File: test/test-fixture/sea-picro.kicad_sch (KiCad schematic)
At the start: 89 parts, among them J2 Sea-Picro

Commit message: tester footprints setup
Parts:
- added H1, H2, H3, H4, H5, H6: M3, MountingHole:MountingHole_3.2mm_M3_Pad_Via, symbol Mechanical:MountingHole_Pad
- added N1: Toggle Clamp, josh-mechanical:GH-201A_X_Adj, symbol Mechanical:Housing
- added R10, R11, R12, R13, R14, R15, R16, R17, R18, R19, R20, R21, R22, R23, R24, R25, R26, R27, R28, R29, R30, R31, R32, R4, R5, R9: 0R0, Resistor_SMD:R_0603_1608Metric, symbol Device:R
- C5: renamed from C?; footprint (none) -> Capacitor_SMD:C_0603_1608Metric
- D2, D3: renamed from D?; footprint (none) -> LED_THT:LED_D5.0mm
- J10, J11, J13, J5, J6: renamed from J?; footprint (none) -> Connector_PinHeader_2.54mm:PinHeader_1x03_P2.54mm_Vertical
- J12: renamed from J?; footprint (none) -> josh-connectors:SAMTEC_FTSH-105-01-L-DV-R-TR
- J2: footprint josh-module:Sea-Picro_EXT_Module_Castellated -> josh-module:Sea-Picro_EXT_Pogo_Pins
- J3, J7: renamed from J?; footprint (none) -> Connector_PinHeader_2.54mm:PinHeader_1x02_P2.54mm_Vertical
- J4: renamed from J?; footprint (none) -> Connector_PinSocket_2.54mm:PinSocket_2x20_P2.54mm_Vertical
- J9: renamed from J?; footprint (none) -> josh-module:OLED_SSD1306_I2C_0.96
- R2, R33, R34, R35, R36, R37, R38, R39, R40, R41, R42, R43, R44, R6, R7, R8: renamed from R?; footprint (none) -> Resistor_SMD:R_0603_1608Metric
- SW1, SW2: renamed from SW?; footprint (none) -> josh-buttons-switches:SW_Push_PTS645
- SW3, SW4, SW5, SW6: renamed from SW?; footprint (none) -> josh-buttons-switches:SW_SPDT_PCM12
- TP1, TP2, TP3, TP4: renamed from TP?; footprint (none) -> josh-test-point:TestPoint_Pogo_1.4mm_Drill_Off_Center
- U1: renamed from U?; footprint (none) -> Package_TO_SOT_SMD:SOT-23-6
- gave numbers to parts that had none: 30
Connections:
- net +5V: now also J9.2 (Pin_2); no longer J9.3 (Pin_3)
- net GND: now also J9.1 (Pin_1), H1.1, H2.1, H3.1, H4.1, H5.1, H6.1; no longer J9.4 (Pin_4)
- net I2C_SCL: now also J9.3 (Pin_3), R12.2; no longer J4.5 (SCL/GPIO3), J9.2 (Pin_2)
- net I2C_SDA: now also J9.4 (Pin_4), R10.2; no longer J4.3 (SDA/GPIO2), J9.1 (Pin_1)
- net LED_FAIL: now also R31.2
- net LED_PASS: now also R32.2
- net LOAD_SW_EN: now also R23.1
- net LOAD_SW_nFAULT: now also R21.1
- net RPI_SWDCLK: now also R27.1; no longer J4.22 (GPIO25)
- net RPI_SWDIO: now also R25.1; no longer J4.18 (GPIO24)
- net RPI_nRST: now also R19.1
- net SEL_BOOTLD: now also R24.2
- net SEL_EXT_RST: now also R22.2
- net SEL_FW: now also R26.2
- net SEL_TEST: now also R28.2
- net SHT_CTRL_3V3: now also R20.2
- net SHT_CTRL_5V: now also R18.2
- net SP_BOOT: now also R30.1
- net SP_RUN: now also R29.1
- net SR_CLK: now also R11.1
- net SR_RCLK: now also R15.1
- net SR_SER: now also R9.1
- net SR_nCLR: now also R13.1
- net SR_nOE: now also R17.1
- net SW_FAIL: now also R16.2
- net SW_PASS: now also R14.2
- net at J4.10 (GPIO15/RXD): now also R5.2
- net at J4.11 (GPIO17): now also R11.2
- net at J4.12 (GPIO18/PWM0): now also R13.2
- net at J4.13 (GPIO27): now also R30.2
- net at J4.15 (GPIO22): now also R21.2
- net at J4.16 (GPIO23): now also R23.2
- net at J4.19 (MOSI0/GPIO10): now also R26.1
- net at J4.21 (MISO0/GPIO9): now also R24.1
- net at J4.23 (SCLK0/GPIO11): now also R28.1
- net at J4.24 (~{CE0}/GPIO8): now also R22.1
- net at J4.26 (~{CE1}/GPIO7): now also R20.1
- net at J4.29 (GCLK1/GPIO5): now also R16.1
- net at J4.31 (GCLK2/GPIO6): now also R18.1
- net at J4.32 (PWM0/GPIO12): now also R31.1
- net at J4.33 (PWM1/GPIO13): now also R32.1
- net at J4.35 (GPIO19/MISO1): now also R15.2
- net at J4.36 (GPIO16): now also R9.2
- net at J4.37 (GPIO26): now also R29.2
- net at J4.38 (GPIO20/MOSI1): now also R17.2
- net at J4.40 (GPIO21/SCLK1): now also R19.2
- net at J4.7 (GCLK0/GPIO4): now also R14.1
- net at J4.8 (GPIO14/TXD): now also R4.2
- new net: J4.3 (SDA/GPIO2), R10.1
- new net: J4.22 (GPIO25), R27.2
- new net: J4.18 (GPIO24), R25.2
- new net: J4.5 (SCL/GPIO3), R12.1
- no-connect marks 13 -> 15
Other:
- moved on the sheet: J9, R6, R7

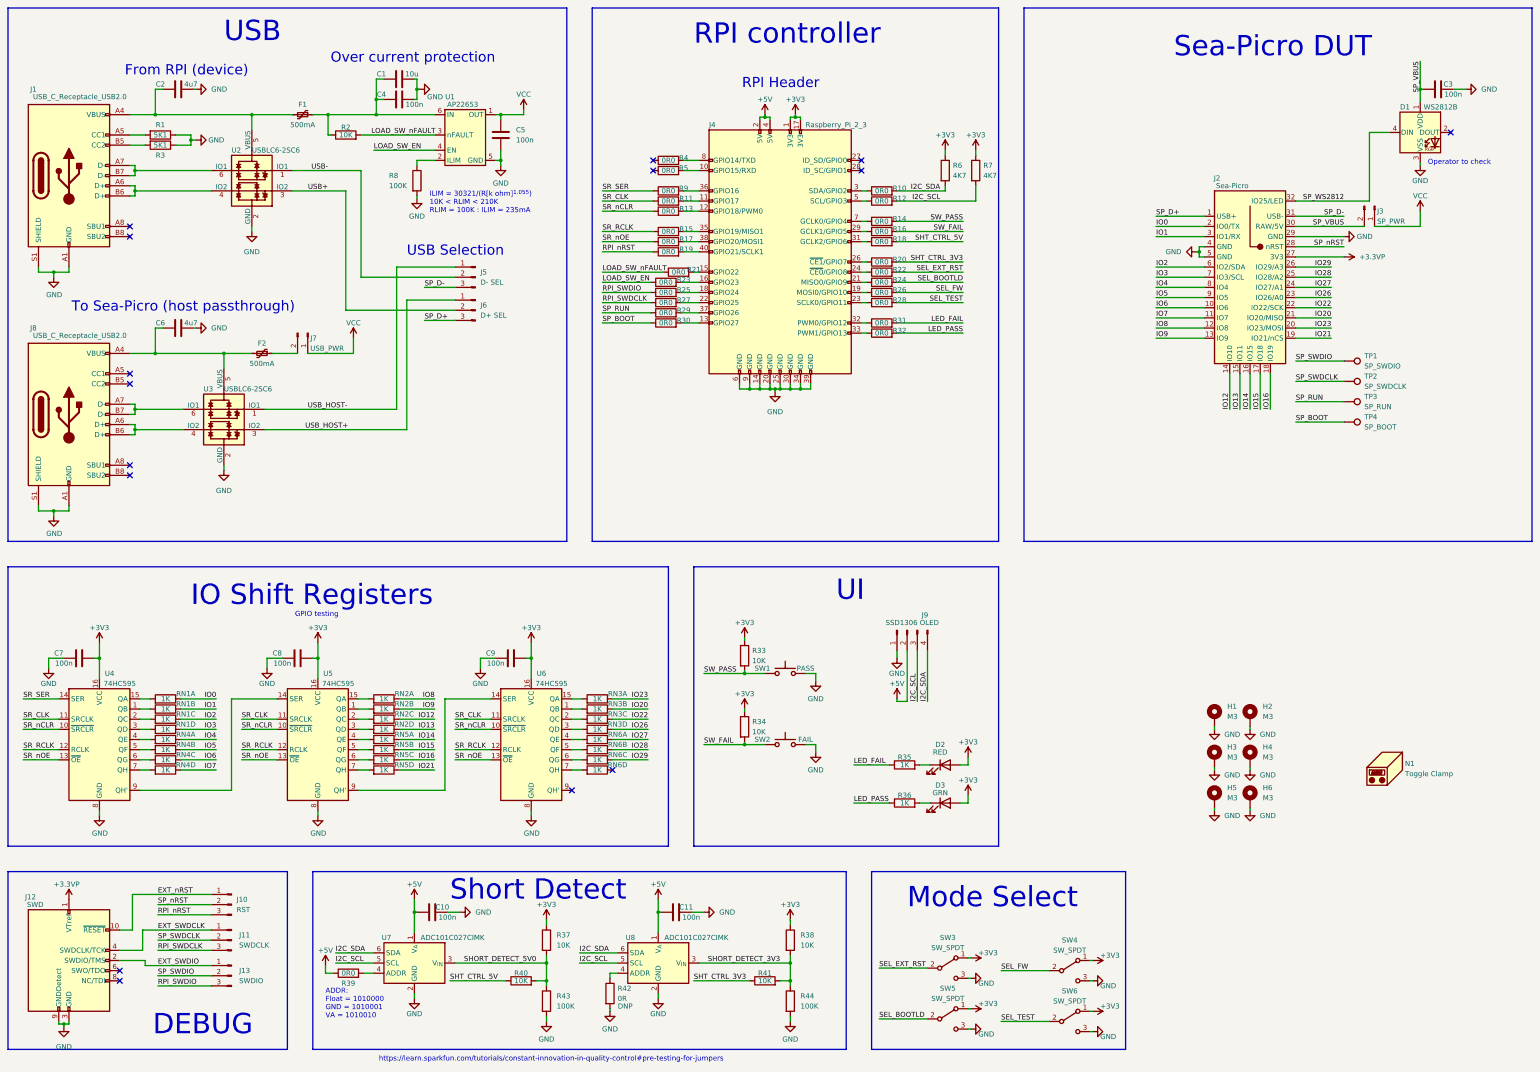
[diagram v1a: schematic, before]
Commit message: rough mechanical layout
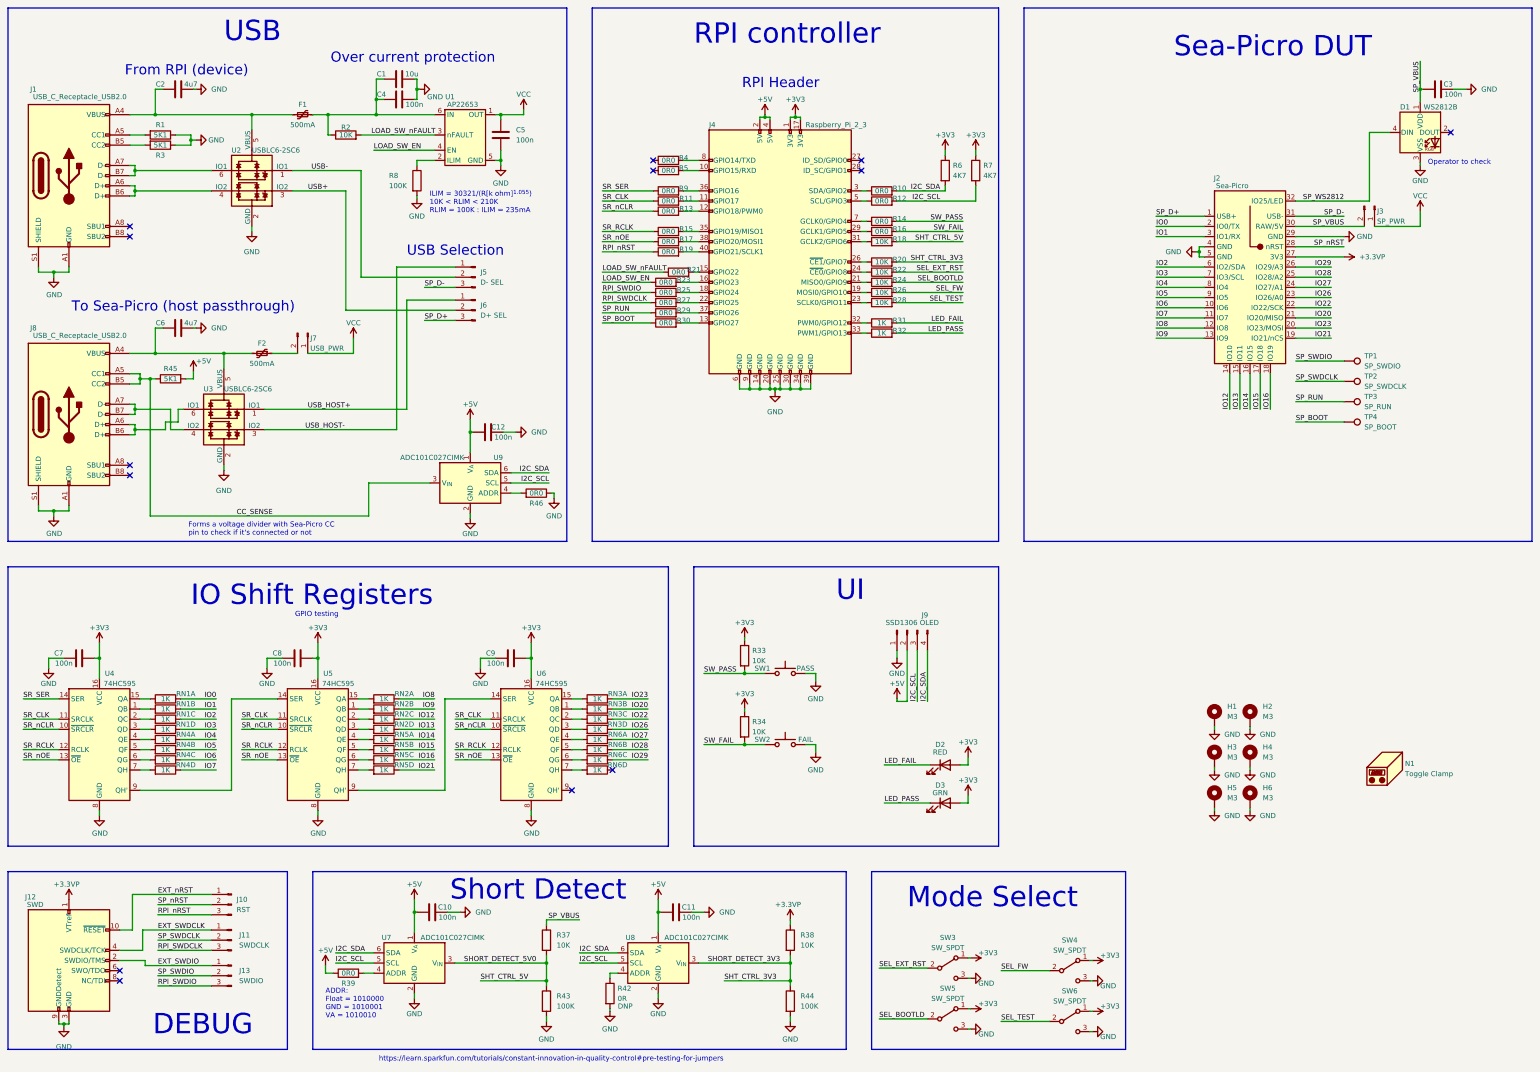
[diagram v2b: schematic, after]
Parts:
- removed R35, R36: 1K, Resistor_SMD:R_0603_1608Metric, symbol Device:R
- removed R40, R41: 10K, Resistor_SMD:R_0603_1608Metric, symbol Device:R
- added C12: 100n, Capacitor_SMD:C_0603_1608Metric, symbol Device:C
- added R45: 5K1, Resistor_SMD:R_0603_1608Metric, symbol Device:R
- added R46: 0R0, Resistor_SMD:R_0603_1608Metric, symbol Device:R
- added U9: ADC101C027CIMK, Package_TO_SOT_SMD:SOT-23-6, symbol Analog_ADC:ADC101C021CIMK
- R18, R20, R22, R24, R26, R28: value 0R0 -> 10K
- R31, R32: value 0R0 -> 1K
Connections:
- net SHT_CTRL_3V3 is gone; now on net SHORT_DETECT_3V3: R20.2
- net SHT_CTRL_5V is gone; now on net SHORT_DETECT_5V0: R18.2
- net +3.3VP: now also R38.1
- net +3V3: no longer R37.1, R38.1
- net +5V: now also C12.1, R45.2, U9.1 (V_{A})
- net GND: now also C12.2, R46.1, U9.2 (GND)
- net I2C_SCL: now also U9.5 (SCL)
- net I2C_SDA: now also U9.6 (SDA)
- net LED_FAIL: now also D2.1 (K)
- net LED_PASS: now also D3.1 (K)
- net SP_VBUS: now also R37.1
- net USB_HOST+: now also U3.1 (IO1); no longer U3.3 (IO2)
- net USB_HOST-: now also U3.3 (IO2); no longer U3.1 (IO1)
- net at J8.A6 (D+), J8.B6 (D+): now also U3.6 (IO1); no longer U3.4 (IO2)
- net at J8.A7 (D-), J8.B7 (D-): now also U3.4 (IO2); no longer U3.6 (IO1)
- net CC_SENSE: now reaches J8.A5 (CC1)
- net CC_SENSE: now also J8.B5 (CC2), R45.1, U9.3 (V_{IN})
- new net: R46.2, U9.4 (ADDR)
- no-connect marks 15 -> 13
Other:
- note added: "Forms a voltage divider with Sea-Picro CC pin to check if it's connected or not"

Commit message: test/quick-test-fixture
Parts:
- added H7: M2, MountingHole:MountingHole_2.2mm_M2_DIN965_Pad, symbol Mechanical:MountingHole_Pad
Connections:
- net +3.3VP: no longer J12.1 (VTref)
- net +3V3: now also J12.1 (VTref)
- net GND: now also H7.1
- net IO0: now also RN4.8; no longer RN1.5
- net IO1: now also RN4.7; no longer RN1.6
- net IO12: now also RN5.6; no longer RN2.7
- net IO13: now also RN5.5; no longer RN2.8
- net IO14: now also RN2.8; no longer RN5.5
- net IO15: now also RN2.7; no longer RN5.6
- net IO16: now also RN2.6; no longer RN5.7
- net IO2: now also RN4.6; no longer RN1.7
- net IO20: now also RN6.6; no longer RN3.6
- net IO21: now also RN2.5; no longer RN5.8
- net IO22: now also RN6.5; no longer RN3.7
- net IO23: now also RN6.7; no longer RN3.5
- net IO27: now also RN3.7; no longer RN6.5
- net IO28: now also RN3.6; no longer RN6.6
- net IO29: now also RN3.5; no longer RN6.7
- net IO3: now also RN4.5; no longer RN1.8
- net IO4: now also RN1.8; no longer RN4.5
- net IO5: now also RN1.7; no longer RN4.6
- net IO6: now also RN1.6; no longer RN4.7
- net IO7: now also RN1.5; no longer RN4.8
- net IO8: now also RN5.8; no longer RN2.5
- net IO9: now also RN5.7; no longer RN2.6
